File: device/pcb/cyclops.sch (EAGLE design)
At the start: 188 parts, among them Q1 NDS351AN, Q2 NDS351AN, Q3 NDS351AN, Q4 IRF510, U1 MCP4921, U10 DG9421, U11 THS4281, U12 MAX4564, U13 ZXTD, U14 ZXTD, U15 OPA1664, U16 LTM8020, U17 DG9421, U2 LT1931, U3 LT1764A, U4 BD00FC0WEFJ, U5 TPS72325, U6 LT1711, U7 TLV3701, U8 ADR03, U9 LT1880

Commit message: Fix silkscreen.
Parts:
- removed D7: 1N5819, jonnew:S-DIODESOD-123
- removed J_ADDR0, J_CS0, J_OC0, J_T0: 0, jonnew:R_0402
- removed R56: 165k, cyclops:R_0603
- added D1: 1N5819, jonnew:S-DIODESOD-123
- added J_ADDR4, J_CS4, J_OC4, J_T4: 0, jonnew:R_0402
- added R51: 220k, cyclops:R_0603
- C10: value 100uF -> JMK212BJ106; device cyclops:C-POL_0807 -> jonnew:C_0805
- C11: value 22uF -> TMK212AB7475KG-T; device cyclops:C_1210 -> jonnew:C_0805
- C12: value 10uF -> 1uF; device jonnew:C_1206 -> cyclops:C_1206
- C13: value 10uF -> 220pF; device jonnew:C_1206 -> cyclops:C_0603
- C14: value 10uF -> 4.7uF; device jonnew:C_1206 -> cyclops:C_1206
- C15: value 10nF -> 10uF; device jonnew:C_0603 -> jonnew:C_1206
- C16: value 10uF -> 10nF; device jonnew:C_1206 -> jonnew:C_0603
- C17: value .1uF -> 10uF; device cyclops:C_0603 -> jonnew:C_1206
- C18: value .1uF -> 22uF; device cyclops:C_0603 -> cyclops:C_1210
- C2: value (none) -> 10uF; device cyclops:C_0603 -> cyclops:C_1206
- C22, C25: value 1uF -> .1uF; device cyclops:C_0805 -> cyclops:C_0603
- C24: value .1uF -> 10nF
- C26, C27, C45: value 0.1uF -> 1uF; device cyclops:C_0603 -> cyclops:C_0805
- C28: value 0.1uF -> .1uF
- C3: value 10uF -> .1uF; device cyclops:C_1206 -> cyclops:C_0603
- C30, C35: value .1uF -> 10uF; device cyclops:C_0603 -> cyclops:C_1206
- C31: value 1uF -> 0.1uF; device cyclops:C_0805 -> cyclops:C_0603
- C32: value 1uF -> 100pF; device cyclops:C_0805 -> cyclops:C_0603
- C33, C39: value 10nF -> 0.1uF
- C37: value 10uF -> 0.1uF; device cyclops:C_1206 -> cyclops:C_0603
- C38: value 10uF -> 6.8nF; device cyclops:C_1206 -> cyclops:C_0603
- C4: value .1uF -> 1uF; device cyclops:C_0603 -> cyclops:C_0805
- C40: value JMK212BJ106 -> 10nF; device jonnew:C_0805 -> cyclops:C_0603
- C41: value TMK212AB7475KG-T -> 10nF; device jonnew:C_0805 -> cyclops:C_0603
- C42: value 100pF -> .1uF
- C43: value 10nF -> 1uF; device cyclops:C_0603 -> cyclops:C_0805
- C44: value 6.8nF -> .1uF
- C5: value 1uF -> (none); device cyclops:C_0805 -> cyclops:C_0603
- C6: value 4.7uF -> 10uF; device cyclops:C_1206 -> jonnew:C_1206
- C7: value 100uF -> 10uF; device cyclops:C-POL_0807 -> jonnew:C_1206
- C8: value 1uF -> 100uF; device cyclops:C_1206 -> cyclops:C-POL_0807
- C9: value 220pF -> 100uF; device cyclops:C_0603 -> cyclops:C-POL_0807
- D2: value 1N5819 -> SZMM3Z5V1; device jonnew:S-DIODESOD-123 -> cyclops:Z-DIODE_SOD-323
- D3: value SZMM3Z5V1 -> STPS0560Z; device cyclops:Z-DIODE_SOD-323 -> jonnew:S-DIODESOD-123
- D4: value MBR0520L -> STPS0560Z; device cyclops:S-DIODESOD-123 -> jonnew:S-DIODESOD-123
- D5: value STPS0560Z -> 1N5819
- D6: value STPS0560Z -> MBR0520L; device jonnew:S-DIODESOD-123 -> cyclops:S-DIODESOD-123
- R1: value 100k -> 10k
- R10: value 100 -> 10k; device jonnew:R_0603 -> cyclops:R_0603
- R11: value 29.4k -> 33k
- R12: value 10k -> 2.2k
- R13: value 10k -> 4.7k
- R15: value 2.2k -> 100k
- R16: value 10k -> 1M
- R17: value 40k -> 165k
- R18: value 100k -> 29.4k
- R19: value 100 -> 10k
- R2: value 10k -> (none)
- R21, R24: value 100k -> 1k
- R26, R30: value 1k -> 100k
- R27: value 1k -> 40k
- R28: value 1k -> 10k
- R3: value 10k -> 100k
- R31: value 470 -> 1k
- R32, R34: value 1k -> 100
- R35: value 220k -> 100k
- R36: value 0 -> 470
- R37: value 0 -> 1k
- R38: value 2.1k -> 1k
- R39, R50: value (none) -> 1k
- R4: value 50 -> 10k; device jonnew:R_1206 -> cyclops:R_0603
- R40: value 1k -> 0
- R41: value 220k -> 1k
- R42: value 50 -> (none)
- R44: value (none) -> 0.5
- R46: value 1k -> 50
- R48: value 0.5 -> 2.1k
- R49: value 0 -> 220k
- R5: value 33k -> 10k
- R52: value 4.7k -> 0
- R53: value 100 -> 0
- R54: value 100k -> (none)
- R55: value 1M -> (none)
- R6: value 50 -> 100; device jonnew:R_1206 -> jonnew:R_0603
- R8: value 10k -> 50; device cyclops:R_0603 -> jonnew:R_1206
- R9: value (none) -> 50; device cyclops:R_0603 -> jonnew:R_1206
- U10: value DG9421 -> LT1880; device jonnew:SPST_IC_SOT23-6 -> jonnew:OPAMP_SOT-23
- U11: value THS4281 -> ZXTD; device jonnew:OPAMP_SOT-23 -> cyclops:ZXTD4591E6
- U12: value MAX4564 -> DG9421; device cyclops:MAX4564 -> jonnew:SPST_IC_SOT23-6
- U13: value ZXTD -> THS4281; device cyclops:ZXTD4591E6 -> jonnew:OPAMP_SOT-23
- U15: value OPA1664 -> DG9421; device jonnew:QUAD-OPAMP_14PIND -> jonnew:SPST_IC_SOT23-6
- U16: value LTM8020 -> MAX4564; device jonnew:LTM8020IVPBF -> cyclops:MAX4564
- U17: value DG9421 -> OPA1664; device jonnew:SPST_IC_SOT23-6 -> jonnew:QUAD-OPAMP_14PIND
- U2: value LT1931 -> LT1764A; device cyclops:LT1611 -> cyclops:LT1963_DDPAK
- U3: value LT1764A -> BD00FC0WEFJ; device cyclops:LT1963_DDPAK -> jonnew:LDO_ADJUST_BDXXFC0
- U4: value BD00FC0WEFJ -> LTM8020; device jonnew:LDO_ADJUST_BDXXFC0 -> jonnew:LTM8020IVPBF
- U5: value TPS72325 -> LT1931; device jonnew:LDO_ADJUST_TPS72325 -> cyclops:LT1611
- U6: value LT1711 -> TPS72325; device jonnew:LT1711 -> jonnew:LDO_ADJUST_TPS72325
- U8: value ADR03 -> LT1711; device cyclops:ADR03AKSZ-REEL7 -> jonnew:LT1711
- U9: value LT1880 -> ADR03; device jonnew:OPAMP_SOT-23 -> cyclops:ADR03AKSZ-REEL7
- renumbered BWFULL<>BWLIM to LIM<BW>FULL, J_LDAC0 to J_LDAC4, J_VI0 to J_VI4, REF2V5 to REF2V1, REF5V0 to REF5V1
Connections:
- net +13.3V: now also C29.1, C30.1, C6.1, C9.+, R10.2, R12.2, R41.1, U11G$1.C, U13G$2.V+, U2.VO, U3.EN, U3.VI; no longer C10.+, C12.1, C34.1, C38.1, R13.2, R15.2, R45.1, U11G$2.V+, U13G$1.C, U3.VO, U4.EN, U4.VI
- net +15V: now also C8.+, D5.A, R15.2, R16.1, U2.VI, U2.~SHDN; no longer C7.+, D7.A, R54.2, R55.1, U3.VI, U3.~SHDN
- net +3V3: now also R1.2, R4.1, R5.1; no longer R2.1, R3.1, R8.2
- net +5V: now also C10.1, C14.1, D1.A, U4.BIAS, U4.VOUT, U4.VOUT_2, U4.VOUT_3, U4.VOUT_4, U4.VOUT_5, U4.VOUT_6, U5.VIN, U5.~SHDN; no longer C40.1, C6.1, D2.A, U16.BIAS, U16.VOUT, U16.VOUT_2, U16.VOUT_3, U16.VOUT_4, U16.VOUT_5, U16.VOUT_6, U2.VIN, U2.~SHDN
- net +6V: now also C26.1, C27.1, C3.1, C37.1, C40.1, C42.1, C43.1, C7.1, D3.C, R11.2, R21.2, R22.2, R31.2, R51.2, U10G$2.V+, U15.V+, U16.V+, U17P.V+, U3.VO, U8G$2.V+, U9.VIN; no longer C14.1, C19.1, C23.1, C24.1, C29.1, C39.1, C45.1, C5.1, D5.C, R26.2, R27.2, R30.2, R35.2, R5.2, U10.V+, U15P.V+, U17.V+, U4.VO, U6G$2.V+, U8.VIN, U9G$2.V+
- net -2.5V: now also C17.2, C23.1, C34.1, C39.1, C41.1, C44.1, C45.1, R49.1, R50.2, U11G$2.C, U13G$2.V-, U15.V-, U16.V-, U17P.V-, U6.VO, U8G$2.V-; no longer C16.2, C21.1, C26.1, C27.1, C30.1, C32.1, C37.1, R41.1, R46.2, U10.V-, U11G$2.V-, U13G$2.C, U15P.V-, U17.V-, U5.VO, U6G$2.V-
- net -5V: now also C15.2, U6.EN, U6.VI; no longer C13.2, U5.EN, U5.VI
- net ADDR0: now also J_ADDR1.2; no longer J_ADDR0.2
- net ADDR1: now also J_ADDR2.2; no longer J_ADDR1.2
- net ADDR2: now also J_ADDR3.2; no longer J_ADDR2.2
- net ADDR3: now also J_ADDR4.2; no longer J_ADDR3.2
- net COM: now also C38.1, U13G$1.-IN, U16.COM; no longer C44.1, U11G$1.-IN, U12.COM
- net COMP+: now also C19.1, R20.1; no longer C17.1, R16.1
- net CS: now also J_CS2.1, J_CS4.2; no longer J_CS0.1, J_CS2.2
- net CS0: now also J_CS2.2; no longer J_CS0.2
- net CS2: now also J_CS3.1; no longer J_CS2.1
- net CS3: now also J_CS4.1; no longer J_CS3.1
- net DACA: now also R2.2; no longer R9.2
- net GND: now also C10.2, C15.1, C16.2, C17.1, C42.2, C44.2, C7.2, C8.-, C9.-, D2.A, D4.A, D6.C, J_ADDR4.1, R13.1, R16.2, R17.1, R26.1, R28.2, R35.1, R38.2, R39.1, R42.2, R54.2, U10G$2.V-, U15.GND, U16.~EN, U4.GND_10, U4.GND_2, U4.GND_3, U4.GND_4, U4.GND_5, U4.GND_6, U4.GND_7, U4.GND_8, U4.GND_9, U6.GND, U8G$1.GND, U8G$1.LATCH, U9.GND; no longer C10.-, C12.2, C13.1, C15.2, C16.1, C17.2, C32.2, C38.2, C7.-, D3.A, D4.C, D6.A, J_ADDR0.1, R12.1, R20.2, R24.1, R29.1, R33.2, R39.2, R44.2, R50.2, R52.1, R56.1, U10.GND, U12.~EN, U16.GND_10, U16.GND_2, U16.GND_3, U16.GND_4, U16.GND_5, U16.GND_6, U16.GND_7, U16.GND_8, U16.GND_9, U17.GND, U6G$1.GND, U6G$1.LATCH, U8.GND, U9G$2.V-
- net IN: now also U16.IN; no longer U12.IN
- net IN1: now also U15.IN; no longer U17.IN
- net ISENSE: now also U16.NC, U17A.+IN, U17C.+IN; no longer U12.NC, U15A.+IN, U15C.+IN
- net LDAC1: now also J_LDAC3.2; no longer J_LDAC1.2
- net LDAC3: now also J_LDAC1.2; no longer J_LDAC3.2
- net LED_ACTIVE: now also R33.2, U8G$1.~Q; no longer R23.2, U6G$1.~Q
- net N$1: now also C5.1, R2.1; no longer C2.1, R9.1
- net N$10: now also R50.1, U11G$2.B, U14G$1.E; no longer R46.1, U13G$1.E, U14G$2.B
- net N$11: now also R53.1, R55.1, U17A.-IN; no longer R49.1, R50.1, U15A.-IN
- net N$12: now also R10.1, U2.ADJ; no longer R13.1, U3.ADJ
- net N$13: now also C32.1, R46.1, U13G$1.OUT, U15.S; no longer C42.1, R42.1, U11G$1.OUT, U17.S
- net N$14: now also R6.1; no longer R10.1
- net N$15: now also R52.1, R54.1, U17C.-IN; no longer R43.1, R44.1, U15C.-IN
- net N$16: now also C32.2, R46.2, U14G$1.B, U14G$2.B; no longer C42.2, R42.2, U13G$1.B, U13G$2.B
- net N$18: now also R37.2, R38.1, U10G$1.-IN; no longer R33.1, R34.2, U9G$1.-IN
- net N$2: now also R21.1; no longer R26.1
- net N$20: now also R36.2, U9.TRIM; no longer R31.2, U8.TRIM
- net N$21: now also C11.1, D5.C, U4.VIN, U4.VIN_2; no longer C41.1, D7.C, U16.VIN, U16.VIN_2
- net N$22: now also R36.1; no longer R31.1
- net N$23: now also R15.1, U4.~SHDN; no longer R54.1, U16.~SHDN
- net N$24: now also R47.1, U11G$2.E; no longer R48.1, U14G$2.E
- net N$25: now also R44.1, U11G$1.E; no longer R47.1, U14G$1.E
- net N$26: now also R44.2; no longer R48.2
- net N$27: now also R24.2; no longer R22.2
- net N$28: now also Q2.G, R24.1, R26.2; no longer Q1.G, R22.1, R24.2
- net N$3: now also R12.1; no longer R15.1
- net N$32: now also C12.1, U5.SW; no longer C8.1, U2.SW
- net N$33: now also C12.2, D6.A; no longer C8.2, D4.A
- net N$35: now also C13.1, C18.1, R18.2; no longer C11.1, C9.1, R11.2
- net N$36: now also C13.2, R18.1, R19.2, U5.NFB; no longer C9.2, R11.1, R12.2, U2.NFB
- net N$37: now also R45.1; no longer R40.1
- net N$38: now also R17.2, U4.ADJ; no longer R56.2, U16.ADJ
- net N$39: now also Q1.G, R23.1, R25.2; no longer Q3.G, R28.1, R29.2
- net N$4: now also R41.2, U11G$1.B, U14G$2.E; no longer R45.2, U13G$2.E, U14G$1.B
- net N$40: now also C38.2, U15.D; no longer C44.2, U17.D
- net N$41: now also Q1.D, R22.1; no longer Q3.D, R30.1
- net N$42: now also R29.1, R30.1, R32.2, U8G$1.+IN; no longer R18.1, R19.2, R21.1, U6G$1.+IN
- net N$43: now also R11.1, R13.2, U3.ADJ/NR; no longer R5.1, R52.2, U4.ADJ/NR
- net N$46: now also R31.1; no longer R27.1
- net N$47: now also Q3.D; no longer Q2.D
- net N$49: now also Q3.G, R33.1, R35.2; no longer Q2.G, R23.1, R25.2
- net N$5: now also C21.1, R27.2, R28.1; no longer C18.1, R17.2, R20.1
- net N$51: now also C16.1, U6.ADJ/NR; no longer C15.1, U5.ADJ/NR
- net N$52: now also R8.1; no longer R4.1
- net N$54: now also R7.1; no longer R6.1
- net N$55: now also R9.1; no longer R7.1
- net N$58: now also L2.1; no longer L1.1
- net N$6: now also R39.2; no longer R32.2
- net N$7: now also C24.1, R34.2, U8G$1.-IN; no longer C43.1, R53.2, U6G$1.-IN
- net N$8: now also R40.1, R42.1, U17D.-IN; no longer R36.1, R39.1, U15D.-IN
- net N$9: now also Q2.D; no longer Q1.D
- net REF2.5: now also C2.1, U10G$1.+IN, U9.VOUT; no longer C3.1, U8.VOUT, U9G$1.+IN
- net REF5.0: now also R27.1, R29.2, R37.1, U10G$1.OUT; no longer R17.1, R18.2, R34.1, U9G$1.OUT
- net SCL: now also R4.2; no longer R2.2
- net SDA: now also R5.2; no longer R3.2
- net T0: now also J_T1.1; no longer J_T0.1
- net T1: now also J_T2.1; no longer J_T1.1
- net T2: now also J_T3.1; no longer J_T2.1
- net T3: now also J_T4.1; no longer J_T3.1
- net TEENSY_VIN: now also D1.C; no longer D2.C
- net TRIG: now also J_T4.2; no longer J_T0.2
- net VAUX: now also D3.A, D4.C, R51.1, U16.NO, U17B.+IN; no longer D5.A, D6.C, R35.1, U12.NO, U15B.+IN
- net VAUX_OUT: now also R8.2, U17B.-IN, U17B.OUT; no longer R4.2, U15B.-IN, U15B.OUT
- net VCTL: now also D2.C, R43.2, R6.2, U12.S; no longer D3.C, R10.2, R37.2, U10.S
- net VCTL_PROT: now also R43.1, R48.2, U12.D; no longer R37.1, R38.2, U10.D
- net VCTL_PROTECT: now also R48.1; no longer R38.1
- net VI: now also R52.2, R7.2, U17C.OUT; no longer R43.2, R6.2, U15C.OUT
- net VI1: now also J_VI3.1; no longer J_VI1.1
- net VI3: now also J_VI1.1; no longer J_VI3.1
- net VI_INTERNAL: now also R20.2, R3.1, R34.1, R53.2, U17A.OUT; no longer R1.1, R16.2, R49.2, R53.1, U15A.OUT
- net VI_LP: now also L2.2, R3.2; no longer L1.2, R1.2
- net VREF: now also R40.2, U17D.OUT; no longer R36.2, U15D.OUT
- net VREF/TTL: now also R9.2; no longer R7.2
- net _VREF: now also R45.2, R49.2, U13G$1.+IN, U17D.+IN; no longer R40.2, R41.2, U11G$1.+IN, U15D.+IN
- net ~LED_ACTIVE: now also R30.2, U8G$1.Q; no longer R21.2, U6G$1.Q
- net ~OC0: now also J_OC1.2; no longer J_OC0.2
- net ~OC1: now also J_OC2.2; no longer J_OC1.2
- net ~OC2: now also J_OC4.2; no longer J_OC2.2
- net ~OVER_CURR: now also L1.1, U12.IN; no longer L2.1, U10.IN
- net ~OVER_CURR_PRE: now also J_OC4.1, L1.2, R1.1, R23.2; no longer J_OC0.1, L2.2, R28.2, R8.1
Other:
- moved on the sheet: C10, C11, C12, C13, C14, C15, C16, C19, C2, C20, C21, C25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

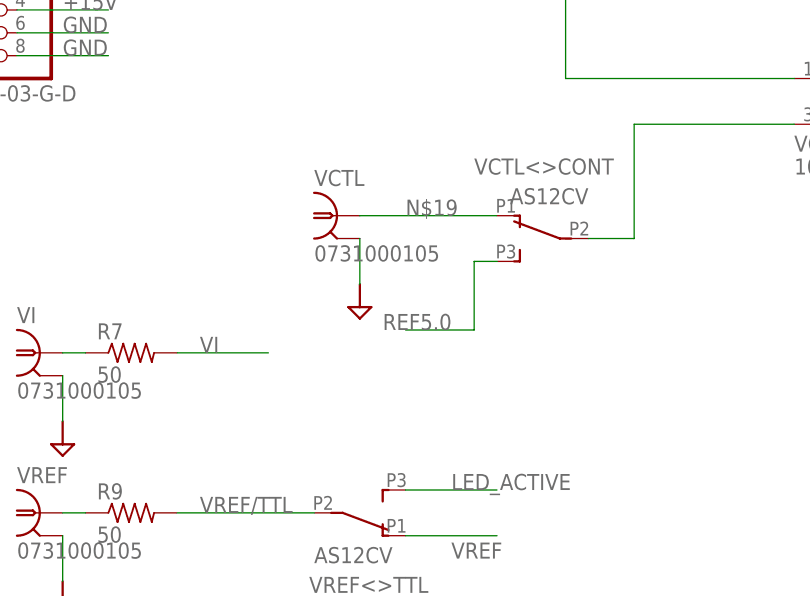
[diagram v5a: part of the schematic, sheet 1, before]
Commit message: Minor fixes after assembly of 3.6
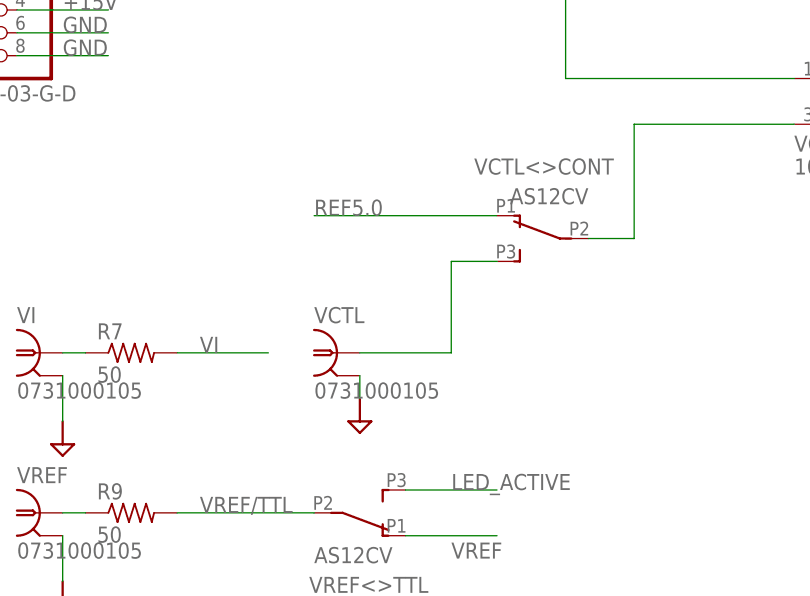
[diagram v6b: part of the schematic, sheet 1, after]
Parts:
- R12: value 2.2k -> 2.1k
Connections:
- net N$19: now also VCTL<>CONT.3; no longer VCTL<>CONT.1
- net REF5.0: now also VCTL<>CONT.1; no longer VCTL<>CONT.3
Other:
- moved on the sheet: VCTL
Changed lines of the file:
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@@
 <?xml version="1.0" encoding="utf-8"?>
 <!DOCTYPE eagle SYSTEM "eagle.dtd">
-<eagle version="6.5.0">
+<eagle version="6.6.0">
 <drawing>
 <settings>
@@
 <part name="REF2V1" library="jonnew" deviceset="TP" device="_RC0603" value="RCU-0C"/>
 <part name="REF5V1" library="jonnew" deviceset="TP" device="_RC0603" value="RCU-0C"/>
-<part name="R12" library="cyclops" deviceset="R" device="_0603" value="2.2k"/>
+<part name="R12" library="cyclops" deviceset="R" device="_0603" value="2.1k"/>
 <part name="R28" library="cyclops" deviceset="R" device="_0603" value="10k"/>
 <part name="R27" library="cyclops" deviceset="R" device="_0603" value="40k"/>
@@
 <instance part="VI" gate="G$1" x="96.52" y="-33.02"/>
 <instance part="VREF" gate="G$1" x="96.52" y="-50.8"/>
-<instance part="VCTL" gate="G$1" x="129.54" y="-17.78"/>
+<instance part="VCTL" gate="G$1" x="129.54" y="-33.02"/>
 <instance part="PWR_DIST" gate="G$1" x="88.9" y="5.08"/>
 <instance part="VCTL&lt;OFF&gt;DAC" gate="G$1" x="187.96" y="-5.08" smashed="yes" rot="MR0">
@@
 <instance part="U$35" gate="G$1" x="251.46" y="22.86"/>
 <instance part="U$36" gate="G$1" x="53.34" y="-60.96"/>
-<instance part="U$37" gate="G$1" x="132.08" y="-27.94"/>
+<instance part="U$37" gate="G$1" x="132.08" y="-40.64"/>
 <instance part="U$38" gate="G$1" x="7.62" y="-60.96"/>
 <instance part="U$39" gate="G$1" x="99.06" y="-43.18"/>
@@
 <segment>
 <pinref part="VCTL" gate="G$1" pin="2"/>
-<wire x1="132.08" y1="-20.32" x2="132.08" y2="-25.4" width="0.1524" layer="91"/>
+<wire x1="132.08" y1="-35.56" x2="132.08" y2="-38.1" width="0.1524" layer="91"/>
 </segment>
 <segment>
@@
 </segment>
 <segment>
-<pinref part="VCTL&lt;&gt;CONT" gate="G$1" pin="3"/>
-<wire x1="147.32" y1="-22.86" x2="144.78" y2="-22.86" width="0.1524" layer="91"/>
-<wire x1="144.78" y1="-22.86" x2="144.78" y2="-30.48" width="0.1524" layer="91"/>
-<wire x1="144.78" y1="-30.48" x2="137.16" y2="-30.48" width="0.1524" layer="91"/>
-<label x="134.62" y="-30.48" size="1.778" layer="95"/>
+<wire x1="147.32" y1="-17.78" x2="127" y2="-17.78" width="0.1524" layer="91"/>
+<label x="127" y="-17.78" size="1.778" layer="95"/>
+<pinref part="VCTL&lt;&gt;CONT" gate="G$1" pin="1"/>
 </segment>
 </net>
@@
 <segment>
 <pinref part="VCTL" gate="G$1" pin="1"/>
-<label x="137.16" y="-17.78" size="1.778" layer="95"/>
-<pinref part="VCTL&lt;&gt;CONT" gate="G$1" pin="1"/>
-<wire x1="147.32" y1="-17.78" x2="132.08" y2="-17.78" width="0.1524" layer="91"/>
-</segment>
-</net>
+<wire x1="132.08" y1="-33.02" x2="142.24" y2="-33.02" width="0.1524" layer="91"/>
+<wire x1="142.24" y1="-33.02" x2="142.24" y2="-22.86" width="0.1524" layer="91"/>
+<pinref part="VCTL&lt;&gt;CONT" gate="G$1" pin="3"/>
+<wire x1="142.24" y1="-22.86" x2="147.32" y2="-22.86" width="0.1524" layer="91"/>
+</segment>
+</net>

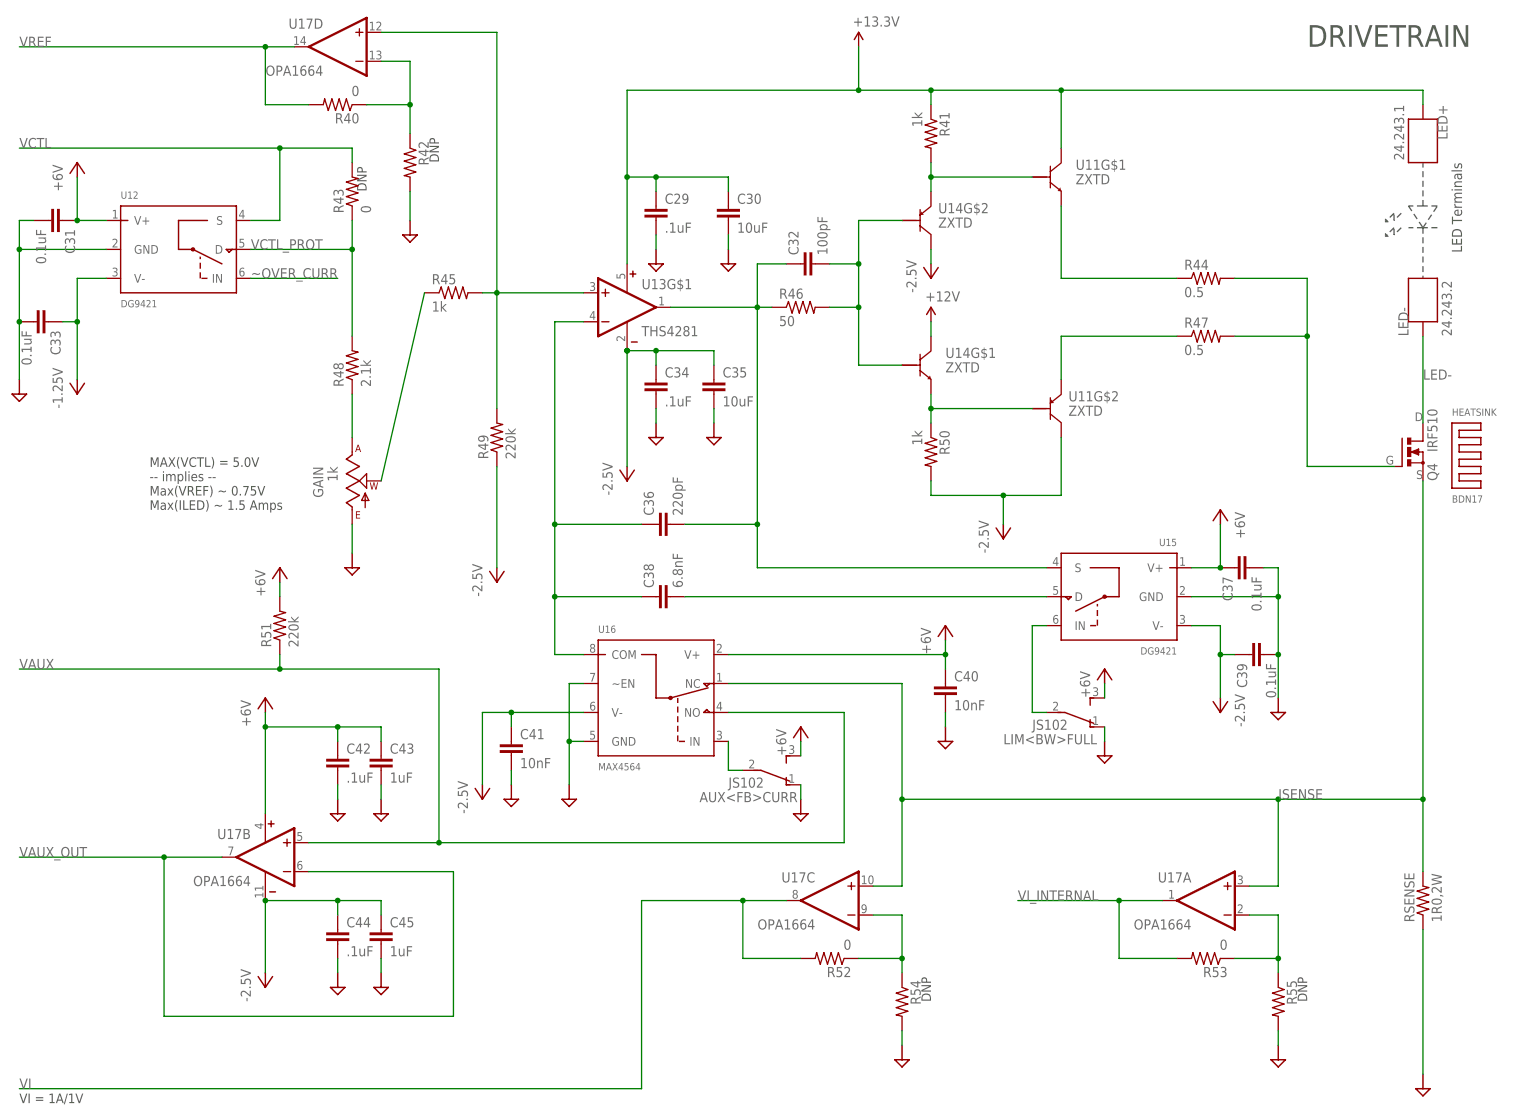
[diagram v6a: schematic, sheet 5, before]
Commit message: Final fixes for 3.6
- Fixed issue with parasitic oscillation in BJT booster stage
- Fixed issue with bandwidth limit selection by simply removing cold
  switch and using the straight panel switch -- extra trace length does
  not matter because it engages the BW limit (self correcting)
- Should be ready for production and master merge
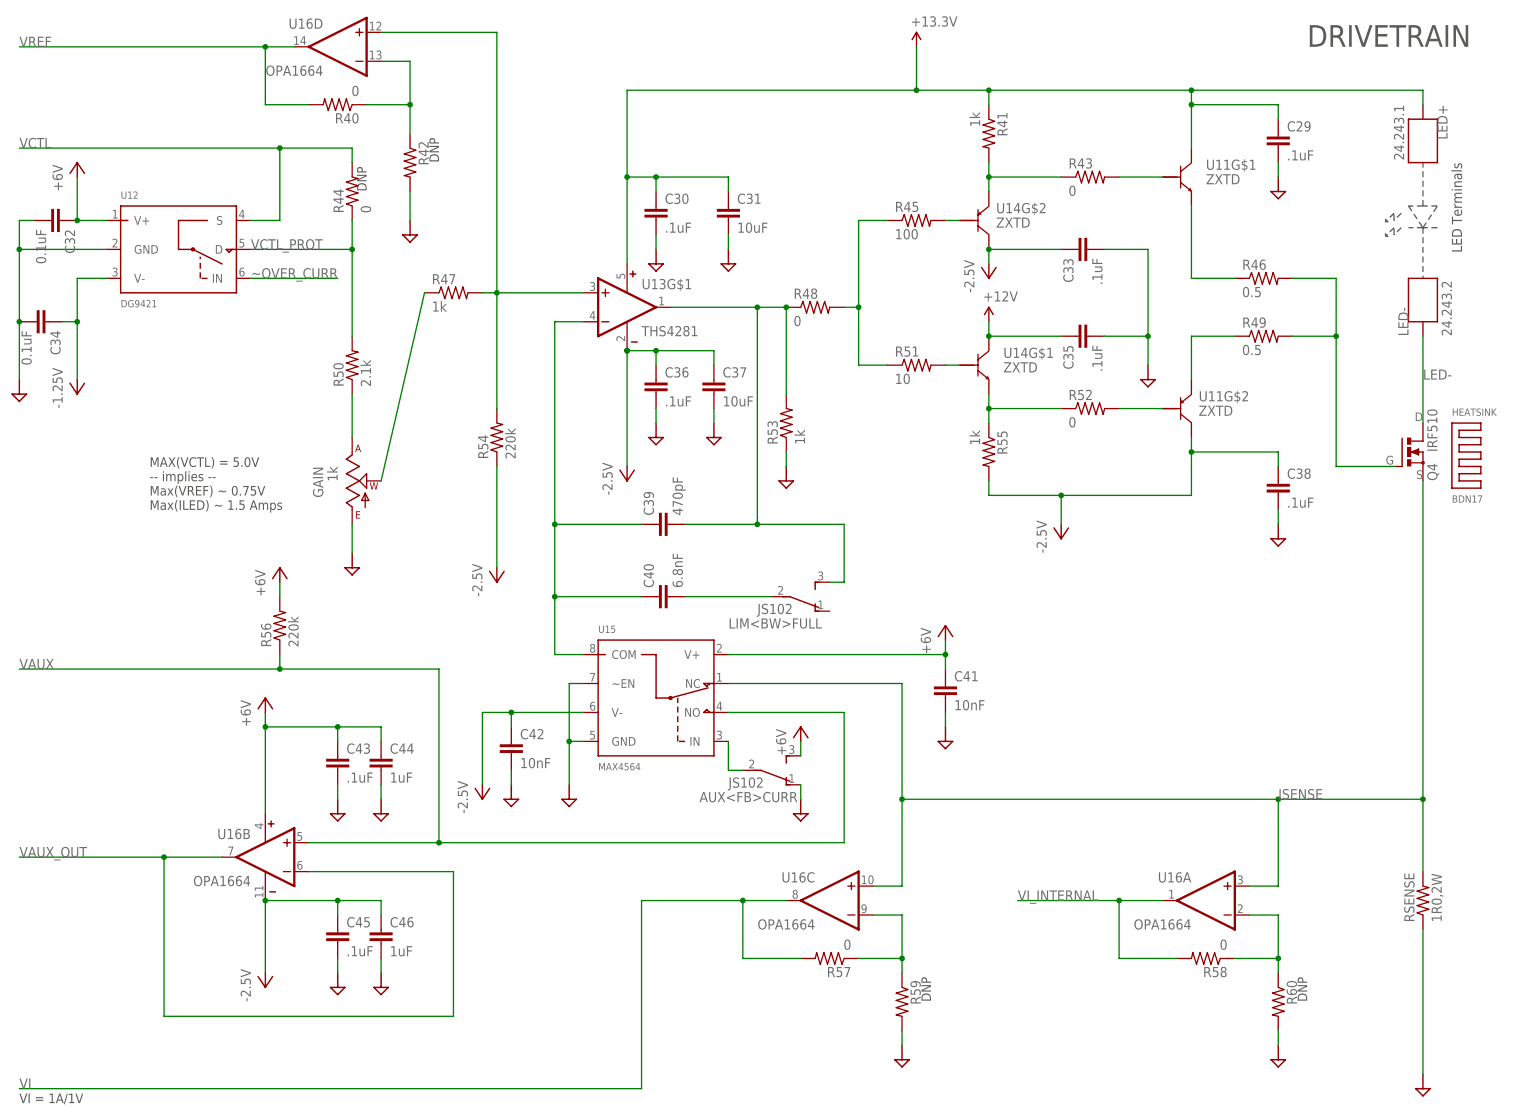
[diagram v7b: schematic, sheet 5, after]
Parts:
- removed U17: OPA1664, jonnew:QUAD-OPAMP_14PIND
- added C46: 1uF, cyclops:C_0805
- added R56: 220k, cyclops:R_0603
- added R57, R58: 0, cyclops:R_0603
- added R59, R60: (no value), cyclops:R_0603
- C29: device cyclops:C_0603 -> jonnew:C_0603
- C30, C35: value 10uF -> .1uF; device cyclops:C_1206 -> cyclops:C_0603
- C31, C37: value 0.1uF -> 10uF; device cyclops:C_0603 -> cyclops:C_1206
- C32: value 100pF -> 0.1uF
- C33: value 0.1uF -> .1uF
- C34: value .1uF -> 0.1uF
- C36: value 220pF -> .1uF
- C38: value 6.8nF -> .1uF; device cyclops:C_0603 -> jonnew:C_0603
- C39: value 0.1uF -> 470pF
- C40: value 10nF -> 6.8nF
- C42: value .1uF -> 10nF
- C43, C45: value 1uF -> .1uF; device cyclops:C_0805 -> cyclops:C_0603
- C44: value .1uF -> 1uF; device cyclops:C_0603 -> cyclops:C_0805
- R44: value 0.5 -> 0
- R45: value 1k -> 100
- R46: value 50 -> 0.5
- R47: value 0.5 -> 1k
- R48: value 2.1k -> 0
- R49: value 220k -> 0.5
- R50: value 1k -> 2.1k
- R51: value 220k -> 10
- R53: value 0 -> 1k
- R54: value (none) -> 220k
- R55: value (none) -> 1k
- U15: value DG9421 -> MAX4564; device jonnew:SPST_IC_SOT23-6 -> cyclops:MAX4564
- U16: value MAX4564 -> OPA1664; device cyclops:MAX4564 -> jonnew:QUAD-OPAMP_14PIND
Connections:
- removed net IN1: LIM<BW>FULL.2, U15.IN
- new net N$44: R52.2, U11G$2.B
- new net N$45: R43.2, U11G$1.B
- new net N$48: R51.2, U14G$1.B
- new net N$50: R45.2, U14G$2.B
- net +13.3V: now also C31.1, C35.1
- net +6V: now also C32.1, C41.1, C44.1, R56.2, U16P.V+; no longer C31.1, C37.1, C40.1, C42.1, LIM<BW>FULL.3, R51.2, U16.V+, U17P.V+
- net -2.5V: now also C36.1, C37.1, C38.1, C42.1, C46.1, R54.1, R55.2, U16P.V-; no longer C35.1, C39.1, C41.1, C44.1, R49.1, R50.2, U16.V-, U17P.V-
- net COM: now also C39.1, C40.1, U15.COM; no longer C36.1, C38.1, U16.COM
- net GND: now also C32.2, C36.2, C38.2, C46.2, R53.1, R59.2, R60.2, U15.~EN; no longer C39.2, C40.2, LIM<BW>FULL.1, R54.2, R55.2, U16.GND, U16.~EN
- net IN: now also U15.IN; no longer U16.IN
- net ISENSE: now also U15.NC, U16A.+IN, U16C.+IN; no longer U16.NC, U17A.+IN, U17C.+IN
- net N$10: now also R52.1, R55.1; no longer R50.1, U11G$2.B
- net N$11: now also R58.1, R60.1, U16A.-IN; no longer R53.1, R55.1, U17A.-IN
- net N$13: now also C39.2, LIM<BW>FULL.3, R48.1, R53.2; no longer C32.1, C36.2, R46.1, U15.S
- net N$15: now also R57.1, R59.1, U16C.-IN; no longer R52.1, R54.1, U17C.-IN
- net N$16: now also R45.1, R48.2, R51.1; no longer C32.2, R46.2, U14G$1.B, U14G$2.B
- net N$24: now also R49.1; no longer R47.1
- net N$25: now also R46.1; no longer R44.1
- net N$26: now also R46.2, R49.2; no longer R44.2, R47.2
- net N$37: now also R47.1; no longer R45.1
- net N$4: now also R43.1; no longer U11G$1.B
- net N$40: now also C40.2, LIM<BW>FULL.2; no longer C38.2, U15.D
- net N$8: now also U16D.-IN; no longer U17D.-IN
- net VAUX: now also R56.1, U15.NO, U16B.+IN; no longer R51.1, U16.NO, U17B.+IN
- net VAUX_OUT: now also U16B.-IN, U16B.OUT; no longer U17B.-IN, U17B.OUT
- net VCTL: now also R44.2; no longer R43.2
- net VCTL_PROT: now also R44.1, R50.2; no longer R43.1, R48.2
- net VCTL_PROTECT: now also R50.1; no longer R48.1
- net VI: now also R57.2, U16C.OUT; no longer R52.2, U17C.OUT
- net VI_INTERNAL: now also R58.2, U16A.OUT; no longer R53.2, U17A.OUT
- net VREF: now also U16D.OUT; no longer U17D.OUT
- net _VREF: now also R47.2, R54.2, U16D.+IN; no longer R45.2, R49.2, U17D.+IN
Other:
- moved on the sheet: C29, C30, C31, C32, C33, C34, C35, C36, C37, C38, C39, C40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
